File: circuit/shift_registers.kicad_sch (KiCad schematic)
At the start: 8 parts, among them U701 74HC595, U702 74HC595, U703 74HC595, U704 74HC595

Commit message: Circuit tweaks and PCB
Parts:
- C701, C704: footprint Capacitor_THT:C_Disc_D3.0mm_W2.0mm_P2.50mm -> Capacitor_THT:C_Disc_D5.0mm_W2.5mm_P2.50mm
- C702: renamed from C703; footprint Capacitor_THT:C_Disc_D3.0mm_W2.0mm_P2.50mm -> Capacitor_THT:C_Disc_D5.0mm_W2.5mm_P2.50mm
- C703: renamed from C702; footprint Capacitor_THT:C_Disc_D3.0mm_W2.0mm_P2.50mm -> Capacitor_THT:C_Disc_D5.0mm_W2.5mm_P2.50mm
- renumbered U703 to U702, U702 to U703
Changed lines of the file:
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@@
 			)
 		)
-		(property "Footprint" "Capacitor_THT:C_Disc_D3.0mm_W2.0mm_P2.50mm"
+		(property "Footprint" "Capacitor_THT:C_Disc_D5.0mm_W2.5mm_P2.50mm"
 			(at 124.46 114.3 0)
 			(effects
@@
 		(dnp no)
 		(fields_autoplaced yes)
-		(property "Reference" "U703"
+		(property "Reference" "U702"
 			(at 73.2633 78.74 0)
 			(effects
@@
 			(project "circuit"
 				(path "/420e3d7a-6c9a-4806-b4be-05d56aeb21de/4760116a-7aa4-465f-87dd-a53dbe30c185"
-					(reference "U703")
+					(reference "U702")
 					(unit 1)
 				)
@@
 		(dnp no)
 		(fields_autoplaced yes)
-		(property "Reference" "C703"
+		(property "Reference" "C702"
 			(at 55.88 110.4962 0)
 			(effects
@@
 			)
 		)
-		(property "Footprint" "Capacitor_THT:C_Disc_D3.0mm_W2.0mm_P2.50mm"
+		(property "Footprint" "Capacitor_THT:C_Disc_D5.0mm_W2.5mm_P2.50mm"
 			(at 53.34 111.76 0)
 			(effects
@@
 			(project "circuit"
 				(path "/420e3d7a-6c9a-4806-b4be-05d56aeb21de/4760116a-7aa4-465f-87dd-a53dbe30c185"
-					(reference "C703")
+					(reference "C702")
 					(unit 1)
 				)
@@
 		(dnp no)
 		(fields_autoplaced yes)
-		(property "Reference" "#PWR0703"
+		(property "Reference" "#PWR0702"
 			(at 50.8 120.65 0)
 			(effects
@@
 			(project "circuit"
 				(path "/420e3d7a-6c9a-4806-b4be-05d56aeb21de/4760116a-7aa4-465f-87dd-a53dbe30c185"
-					(reference "#PWR0703")
+					(reference "#PWR0702")
 					(unit 1)
 				)
@@
 			)
 		)
-		(property "Footprint" "Capacitor_THT:C_Disc_D3.0mm_W2.0mm_P2.50mm"
+		(property "Footprint" "Capacitor_THT:C_Disc_D5.0mm_W2.5mm_P2.50mm"
 			(at 53.34 59.69 0)
 			(effects
@@
 		(dnp no)
 		(fields_autoplaced yes)
-		(property "Reference" "U702"
+		(property "Reference" "U703"
 			(at 132.9533 26.2 0)
 			(effects
@@
 			(project "circuit"
 				(path "/420e3d7a-6c9a-4806-b4be-05d56aeb21de/4760116a-7aa4-465f-87dd-a53dbe30c185"
-					(reference "U702")
+					(reference "U703")
 					(unit 1)
 				)
@@
 		(dnp no)
 		(fields_autoplaced yes)
-		(property "Reference" "#PWR0702"
+		(property "Reference" "#PWR0703"
 			(at 110.49 72.39 0)
 			(effects
@@
 			(project "circuit"
 				(path "/420e3d7a-6c9a-4806-b4be-05d56aeb21de/4760116a-7aa4-465f-87dd-a53dbe30c185"
-					(reference "#PWR0702")
+					(reference "#PWR0703")
 					(unit 1)
 				)
@@
 		(dnp no)
 		(fields_autoplaced yes)
-		(property "Reference" "C702"
+		(property "Reference" "C703"
 			(at 115.57 62.2362 0)
 			(effects
@@
 			)
 		)
-		(property "Footprint" "Capacitor_THT:C_Disc_D3.0mm_W2.0mm_P2.50mm"
+		(property "Footprint" "Capacitor_THT:C_Disc_D5.0mm_W2.5mm_P2.50mm"
 			(at 113.03 63.5 0)
 			(effects
@@
 			(project "circuit"
 				(path "/420e3d7a-6c9a-4806-b4be-05d56aeb21de/4760116a-7aa4-465f-87dd-a53dbe30c185"
-					(reference "C702")
-					(unit 1)
-				)
+					(reference "C703")
+					(unit 1)
+				)

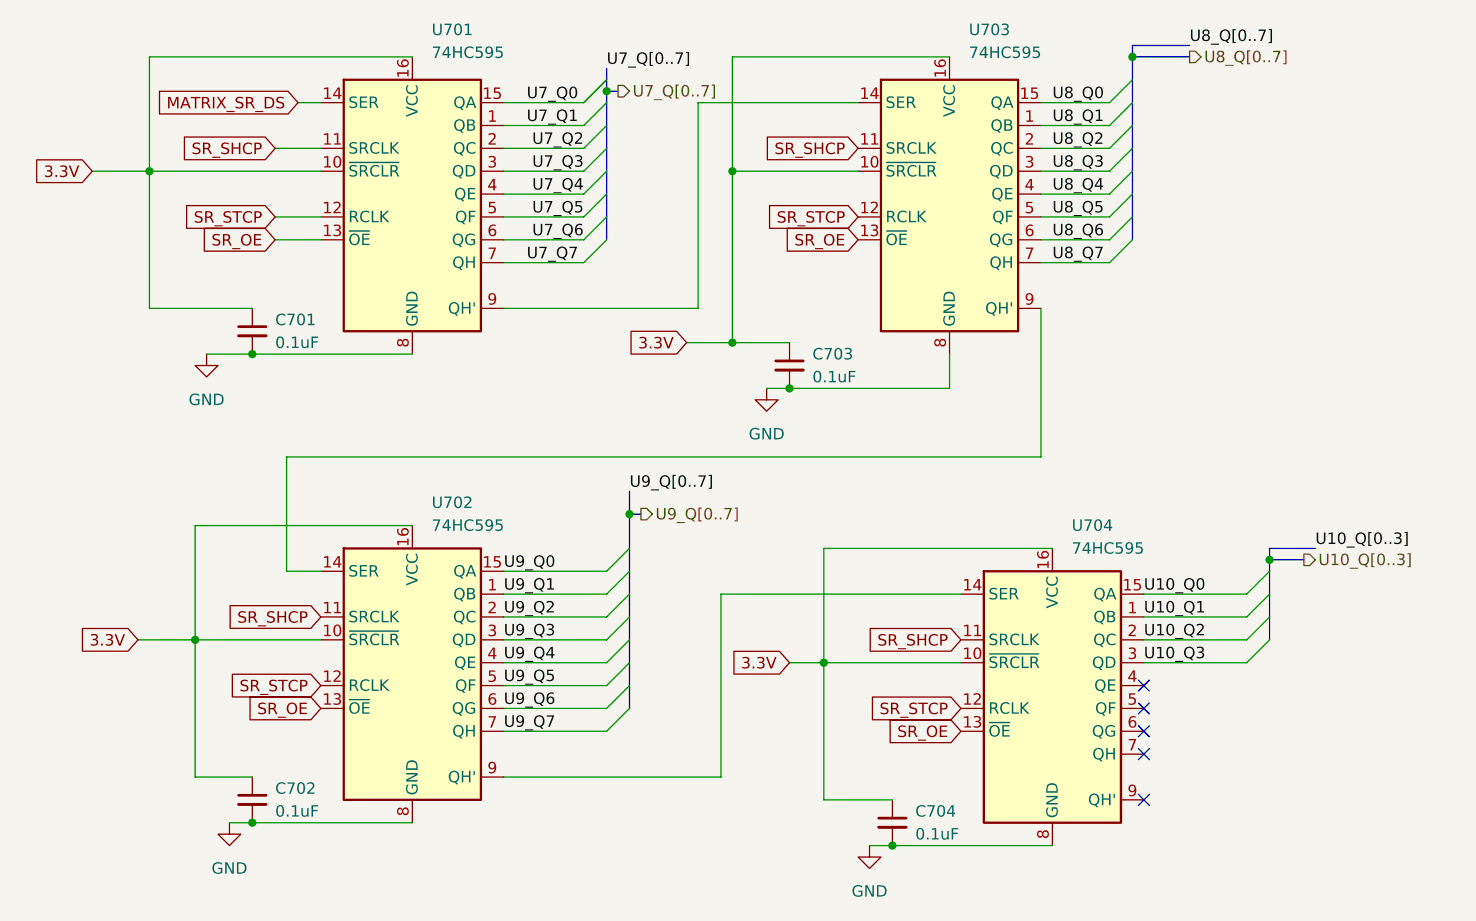
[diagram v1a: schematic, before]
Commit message: Labels for headers on PCB
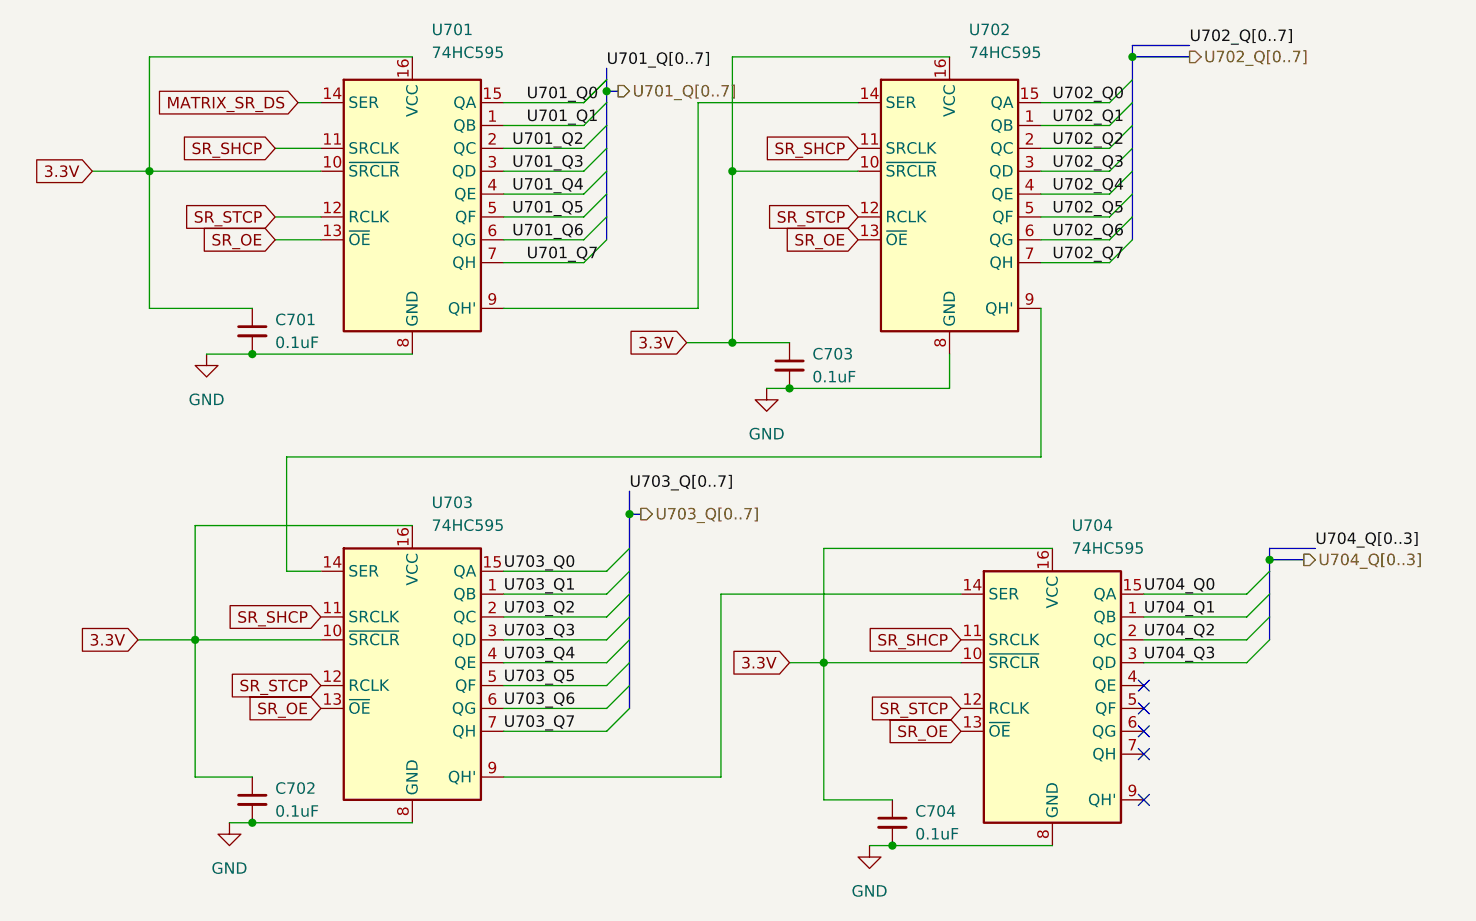
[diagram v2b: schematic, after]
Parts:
- renumbered U703 to U702, U702 to U703
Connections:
- net U10_Q0 renamed U704_Q0
- net U10_Q1 renamed U704_Q1
- net U10_Q2 renamed U704_Q2
- net U10_Q3 renamed U704_Q3
- net U7_Q0 renamed U701_Q0
- net U7_Q1 renamed U701_Q1
- net U7_Q2 renamed U701_Q2
- net U7_Q3 renamed U701_Q3
- net U7_Q4 renamed U701_Q4
- net U7_Q5 renamed U701_Q5
- net U7_Q6 renamed U701_Q6
- net U7_Q7 renamed U701_Q7
- net U8_Q0 renamed U702_Q0
- net U8_Q1 renamed U702_Q1
- net U8_Q2 renamed U702_Q2
- net U8_Q3 renamed U702_Q3
- net U8_Q4 renamed U702_Q4
- net U8_Q5 renamed U702_Q5
- net U8_Q6 renamed U702_Q6
- net U8_Q7 renamed U702_Q7
- net U9_Q0 renamed U703_Q0
- net U9_Q1 renamed U703_Q1
- net U9_Q2 renamed U703_Q2
- net U9_Q3 renamed U703_Q3
- net U9_Q4 renamed U703_Q4
- net U9_Q5 renamed U703_Q5
- net U9_Q6 renamed U703_Q6
- net U9_Q7 renamed U703_Q7
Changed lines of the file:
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@@
 		)
 	)
-	(label "U7_Q1"
+	(label "U701_Q1"
 		(at 83.82 36.83 0)
 		(effects
@@
 		)
 	)
-	(label "U10_Q0"
+	(label "U704_Q0"
 		(at 152.4 88.9 0)
 		(effects
@@
 		)
 	)
-	(label "U8_Q4"
+	(label "U702_Q4"
 		(at 142.24 44.45 0)
 		(effects
@@
 		)
 	)
-	(label "U7_Q0"
+	(label "U701_Q0"
 		(at 83.82 34.29 0)
 		(effects
@@
 		)
 	)
-	(label "U9_Q5"
+	(label "U703_Q5"
 		(at 81.28 99.06 0)
 		(effects
@@
 		)
 	)
-	(label "U7_Q4"
+	(label "U701_Q4"
 		(at 90.17 44.45 180)
 		(effects
@@
 		)
 	)
-	(label "U10_Q2"
+	(label "U704_Q2"
 		(at 152.4 93.98 0)
 		(effects
@@
 		)
 	)
-	(label "U8_Q0"
+	(label "U702_Q0"
 		(at 142.24 34.29 0)
 		(effects
@@
 		)
 	)
-	(label "U10_Q1"
+	(label "U704_Q1"
 		(at 152.4 91.44 0)
 		(effects
@@
 		)
 	)
-	(label "U8_Q[0..7]"
+	(label "U702_Q[0..7]"
 		(at 157.48 27.94 0)
 		(effects
@@
 		)
 	)
-	(label "U8_Q2"
+	(label "U702_Q2"
 		(at 142.24 39.37 0)
 		(effects
@@
 		)
 	)
-	(label "U9_Q3"
+	(label "U703_Q3"
 		(at 81.28 93.98 0)
 		(effects
@@
 		)
 	)
-	(label "U9_Q7"
+	(label "U703_Q7"
 		(at 81.28 104.14 0)
 		(effects
@@
 		)
 	)
-	(label "U7_Q5"
+	(label "U701_Q5"
 		(at 90.17 46.99 180)
 		(effects
@@
 		)
 	)
-	(label "U8_Q1"
+	(label "U702_Q1"
 		(at 142.24 36.83 0)
 		(effects
@@
 		)
 	)
-	(label "U7_Q7"
+	(label "U701_Q7"
 		(at 83.82 52.07 0)
 		(effects
@@
 		)
 	)
-	(label "U9_Q6"
+	(label "U703_Q6"
 		(at 81.28 101.6 0)
 		(effects
@@
 		)
 	)
-	(label "U10_Q3"
+	(label "U704_Q3"
 		(at 152.4 96.52 0)
 		(effects
@@
 		)
 	)
-	(label "U8_Q3"
+	(label "U702_Q3"
 		(at 142.24 41.91 0)
 		(effects
@@
 		)
 	)
-	(label "U7_Q6"
+	(label "U701_Q6"
 		(at 90.17 49.53 180)
 		(effects
@@
 		)
 	)
-	(label "U7_Q2"
+	(label "U701_Q2"
 		(at 90.17 39.37 180)
 		(effects
@@
 		)
 	)
-	(label "U9_Q4"
+	(label "U703_Q4"
 		(at 81.28 96.52 0)
 		(effects
@@
 		)
 	)
-	(label "U8_Q5"
+	(label "U702_Q5"
 		(at 142.24 46.99 0)
 		(effects
@@
 		)
 	)
-	(label "U9_Q0"
+	(label "U703_Q0"
 		(at 81.28 86.36 0)
 		(effects
@@
 		)
 	)
-	(label "U7_Q3"
+	(label "U701_Q3"
 		(at 90.17 41.91 180)
 		(effects
@@
 		)
 	)
-	(label "U8_Q7"
+	(label "U702_Q7"
 		(at 142.24 52.07 0)
 		(effects
@@
 		)
 	)
-	(label "U9_Q[0..7]"
+	(label "U703_Q[0..7]"
 		(at 95.25 77.47 0)
 		(effects
@@
 		)
 	)
-	(label "U10_Q[0..3]"
+	(label "U704_Q[0..3]"
 		(at 171.45 83.82 0)
 		(effects
@@
 		)
 	)
-	(label "U8_Q6"
+	(label "U702_Q6"
 		(at 142.24 49.53 0)
 		(effects
@@
 		)
 	)
-	(label "U7_Q[0..7]"
+	(label "U701_Q[0..7]"
 		(at 92.71 30.48 0)
 		(effects
@@
 		)
 	)
-	(label "U9_Q1"
+	(label "U703_Q1"
 		(at 81.28 88.9 0)
 		(effects
@@
 		)
 	)
-	(label "U9_Q2"
+	(label "U703_Q2"
 		(at 81.28 91.44 0)
 		(effects
@@
 		)
 	)
-	(hierarchical_label "U7_Q[0..7]"
+	(hierarchical_label "U701_Q[0..7]"
 		(shape output)
 		(at 93.98 33.02 0)
@@
 		)
 	)
-	(hierarchical_label "U10_Q[0..3]"
+	(hierarchical_label "U704_Q[0..3]"
 		(shape output)
 		(at 170.18 85.09 0)
@@
 		)
 	)
-	(hierarchical_label "U8_Q[0..7]"
+	(hierarchical_label "U702_Q[0..7]"
 		(shape output)
 		(at 157.48 29.21 0)
@@
 		)
 	)
-	(hierarchical_label "U9_Q[0..7]"
+	(hierarchical_label "U703_Q[0..7]"
 		(shape output)
 		(at 96.52 80.01 0)
@@
 		(dnp no)
 		(fields_autoplaced yes)
-		(property "Reference" "U702"
+		(property "Reference" "U703"
 			(at 73.2633 78.74 0)
 			(effects
@@
 			(project "circuit"
 				(path "/420e3d7a-6c9a-4806-b4be-05d56aeb21de/4760116a-7aa4-465f-87dd-a53dbe30c185"
-					(reference "U702")
+					(reference "U703")
 					(unit 1)
 				)
@@
 		(dnp no)
 		(fields_autoplaced yes)
-		(property "Reference" "U703"
+		(property "Reference" "U702"
 			(at 132.9533 26.2 0)
 			(effects
@@
 			(project "circuit"
 				(path "/420e3d7a-6c9a-4806-b4be-05d56aeb21de/4760116a-7aa4-465f-87dd-a53dbe30c185"
-					(reference "U703")
+					(reference "U702")
 					(unit 1)
 				)
